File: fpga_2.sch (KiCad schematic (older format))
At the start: 1 part

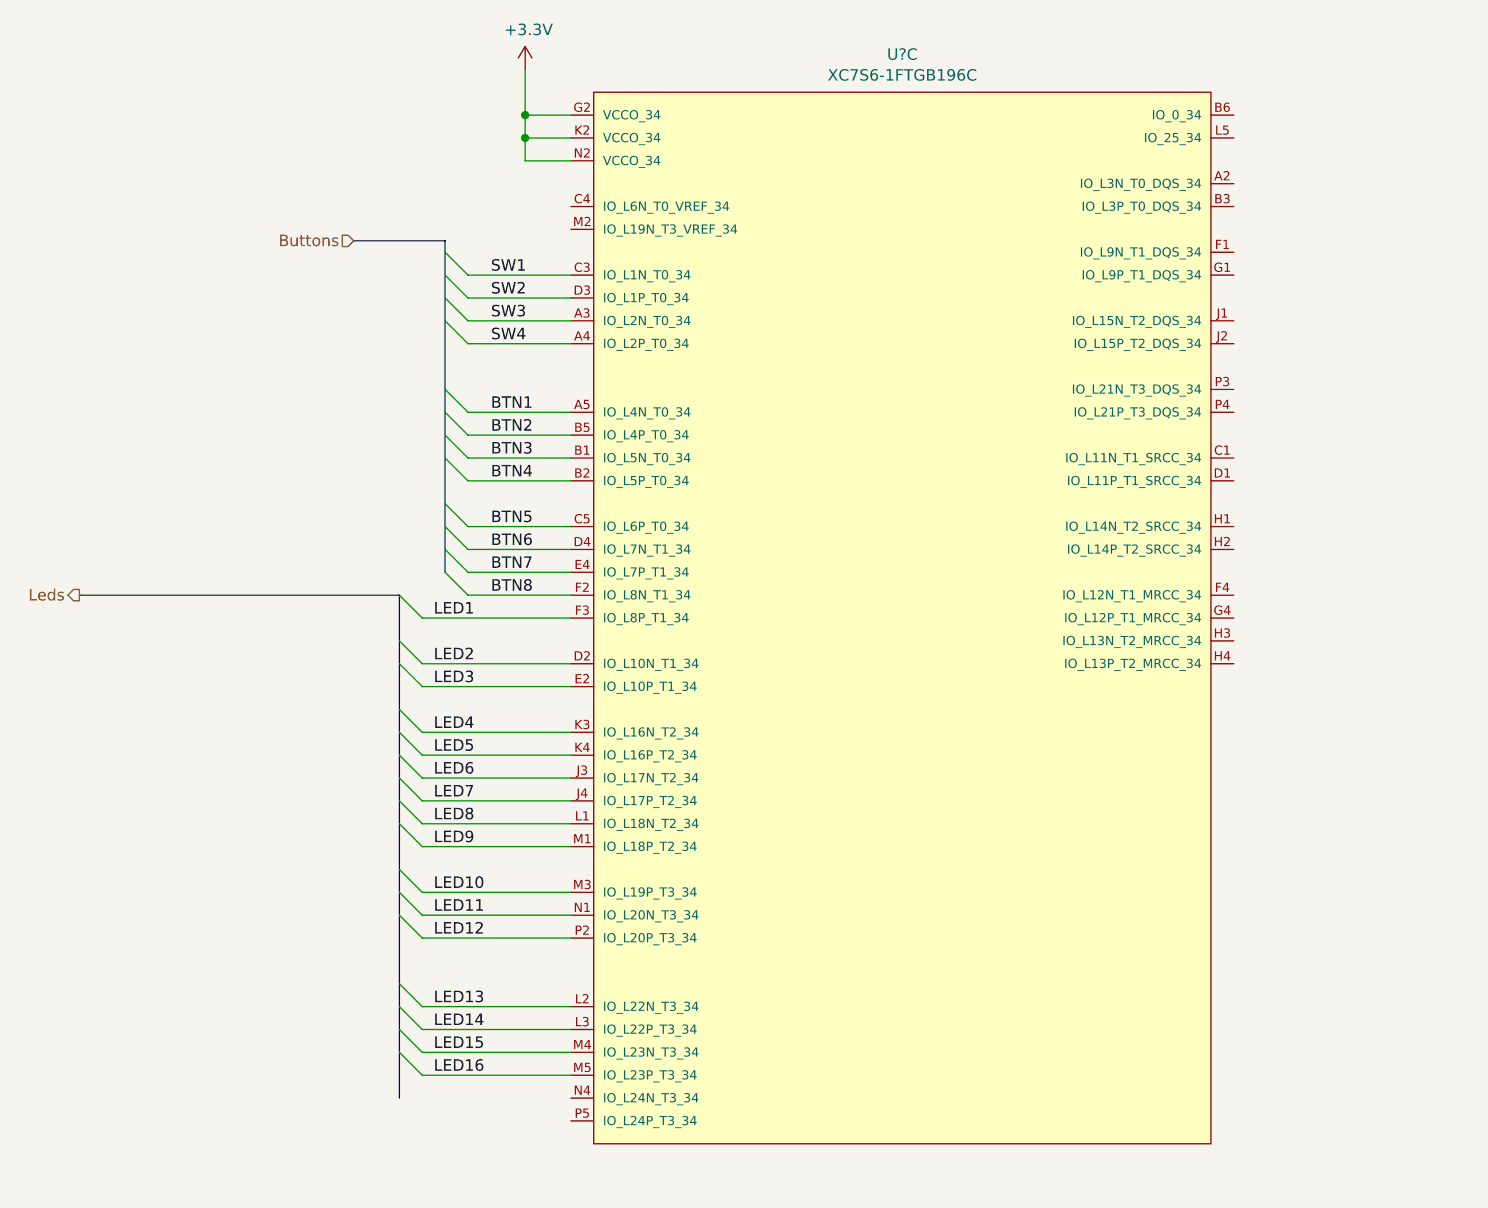
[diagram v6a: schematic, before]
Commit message: Connect USB buses to the FPGA
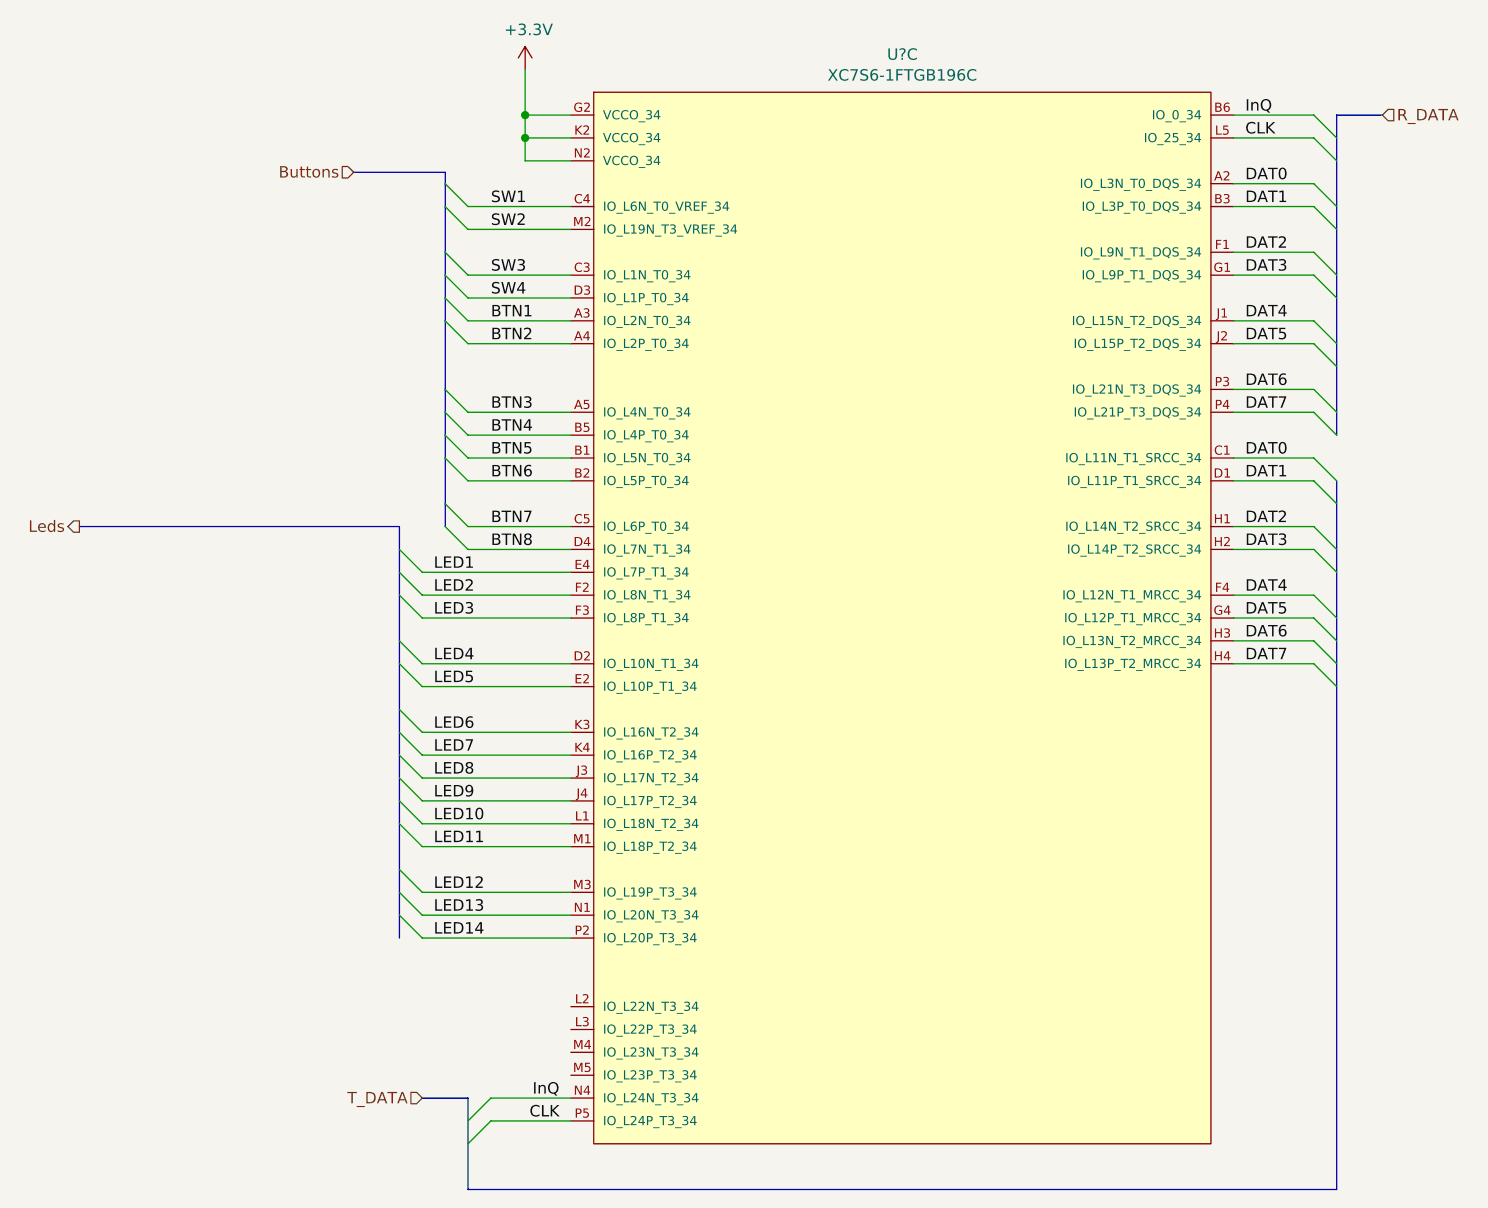
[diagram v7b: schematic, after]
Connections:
- net BTN1: now also U?.A3 (IO_L2N_T0_34); no longer U?.A5 (IO_L4N_T0_34)
- net BTN2: now also U?.A4 (IO_L2P_T0_34); no longer U?.B5 (IO_L4P_T0_34)
- net BTN3: now also U?.A5 (IO_L4N_T0_34); no longer U?.B1 (IO_L5N_T0_34)
- net BTN4: now also U?.B5 (IO_L4P_T0_34); no longer U?.B2 (IO_L5P_T0_34)
- net BTN5: now also U?.B1 (IO_L5N_T0_34); no longer U?.C5 (IO_L6P_T0_34)
- net BTN6: now also U?.B2 (IO_L5P_T0_34); no longer U?.D4 (IO_L7N_T1_34)
- net BTN7: now also U?.C5 (IO_L6P_T0_34); no longer U?.E4 (IO_L7P_T1_34)
- net BTN8: now also U?.D4 (IO_L7N_T1_34); no longer U?.F2 (IO_L8N_T1_34)
- net LED1: now also U?.E4 (IO_L7P_T1_34); no longer U?.F3 (IO_L8P_T1_34)
- net LED10: now also U?.L1 (IO_L18N_T2_34); no longer U?.M3 (IO_L19P_T3_34)
- net LED11: now also U?.M1 (IO_L18P_T2_34); no longer U?.N1 (IO_L20N_T3_34)
- net LED12: now also U?.M3 (IO_L19P_T3_34); no longer U?.P2 (IO_L20P_T3_34)
- net LED13: now also U?.N1 (IO_L20N_T3_34); no longer U?.L2 (IO_L22N_T3_34)
- net LED14: now also U?.P2 (IO_L20P_T3_34); no longer U?.L3 (IO_L22P_T3_34)
- net LED2: now also U?.F2 (IO_L8N_T1_34); no longer U?.D2 (IO_L10N_T1_34)
- net LED3: now also U?.F3 (IO_L8P_T1_34); no longer U?.E2 (IO_L10P_T1_34)
- net LED4: now also U?.D2 (IO_L10N_T1_34); no longer U?.K3 (IO_L16N_T2_34)
- net LED5: now also U?.E2 (IO_L10P_T1_34); no longer U?.K4 (IO_L16P_T2_34)
- net LED6: now also U?.K3 (IO_L16N_T2_34); no longer U?.J3 (IO_L17N_T2_34)
- net LED7: now also U?.K4 (IO_L16P_T2_34); no longer U?.J4 (IO_L17P_T2_34)
- net LED8: now also U?.J3 (IO_L17N_T2_34); no longer U?.L1 (IO_L18N_T2_34)
- net LED9: now also U?.J4 (IO_L17P_T2_34); no longer U?.M1 (IO_L18P_T2_34)
- net SW1: now also U?.C4 (IO_L6N_T0_VREF_34); no longer U?.C3 (IO_L1N_T0_34)
- net SW2: now also U?.M2 (IO_L19N_T3_VREF_34); no longer U?.D3 (IO_L1P_T0_34)
- net SW3: now also U?.C3 (IO_L1N_T0_34); no longer U?.A3 (IO_L2N_T0_34)
- net SW4: now also U?.D3 (IO_L1P_T0_34); no longer U?.A4 (IO_L2P_T0_34)
- net DAT0: now reaches U?.A2 (IO_L3N_T0_DQS_34)
- net DAT0: now also U?.C1 (IO_L11N_T1_SRCC_34)
- net DAT1: now reaches U?.B3 (IO_L3P_T0_DQS_34)
- net DAT1: now also U?.D1 (IO_L11P_T1_SRCC_34)
- net InQ: now reaches U?.B6 (IO_0_34)
- net InQ: now also U?.N4 (IO_L24N_T3_34)
- net DAT2: now reaches U?.F1 (IO_L9N_T1_DQS_34)
- net DAT2: now also U?.H1 (IO_L14N_T2_SRCC_34)
- net DAT4: now reaches U?.F4 (IO_L12N_T1_MRCC_34)
- net DAT4: now also U?.J1 (IO_L15N_T2_DQS_34)
- net DAT3: now reaches U?.G1 (IO_L9P_T1_DQS_34)
- net DAT3: now also U?.H2 (IO_L14P_T2_SRCC_34)
- net DAT5: now reaches U?.G4 (IO_L12P_T1_MRCC_34)
- net DAT5: now also U?.J2 (IO_L15P_T2_DQS_34)
- net DAT6: now reaches U?.H3 (IO_L13N_T2_MRCC_34)
- net DAT6: now also U?.P3 (IO_L21N_T3_DQS_34)
- net DAT7: now reaches U?.H4 (IO_L13P_T2_MRCC_34)
- net DAT7: now also U?.P4 (IO_L21P_T3_DQS_34)
- net CLK: now reaches U?.L5 (IO_25_34)
- net CLK: now also U?.P5 (IO_L24P_T3_34)
- net LED15: no longer names the net of U?.M4 (IO_L23N_T3_34)
- net LED16: no longer names the net of U?.M5 (IO_L23P_T3_34)
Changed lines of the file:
@@
 Wire Wire Line
 	4450 1600 4450 1400
-Text HLabel 3700 2150 0    50   Input ~ 0
+Text HLabel 3700 1850 0    50   Input ~ 0
 Buttons
 Wire Bus Line
-	3700 2150 4100 2150
+	3700 1850 4100 1850
+Entry Wire Line
+	4100 2000 4200 2100
+Entry Wire Line
+	4100 1900 4200 2000
+Entry Wire Line
+	4100 2200 4200 2300
 Entry Wire Line
 	4100 2300 4200 2400
 Entry Wire Line
-	4100 2200 4200 2300
-Entry Wire Line
 	4100 2400 4200 2500
 Entry Wire Line
 	4100 2500 4200 2600
+Wire Wire Line
+	4200 2000 4650 2000
+Wire Wire Line
+	4200 2100 4650 2100
+Wire Wire Line
+	4200 2300 4650 2300
+Wire Wire Line
+	4200 2400 4650 2400
+Wire Wire Line
+	4200 2500 4650 2500
+Wire Wire Line
+	4200 2600 4650 2600
+Text Label 4300 2000 0    50   ~ 0
+SW1
+Text Label 4300 2100 0    50   ~ 0
+SW2
+Text Label 4300 2300 0    50   ~ 0
+SW3
+Text Label 4300 2400 0    50   ~ 0
+SW4
+Text Label 4300 2500 0    50   ~ 0
+BTN1
+Text Label 4300 2600 0    50   ~ 0
+BTN2
 Entry Wire Line
 	4100 2800 4200 2900
 Entry Wire Line
 	4100 2900 4200 3000
-Wire Wire Line
-	4200 2300 4650 2300
-Wire Wire Line
-	4200 2400 4650 2400
-Wire Wire Line
-	4200 2500 4650 2500
-Wire Wire Line
-	4200 2600 4650 2600
+Entry Wire Line
+	4100 3000 4200 3100
+Entry Wire Line
+	4100 3100 4200 3200
+Entry Wire Line
+	4100 3300 4200 3400
+Entry Wire Line
+	4100 3400 4200 3500
 Wire Wire Line
 	4200 2900 4650 2900
 Wire Wire Line
 	4200 3000 4650 3000
-Text Label 4300 2300 0    50   ~ 0
-SW1
-Text Label 4300 2400 0    50   ~ 0
-SW2
-Text Label 4300 2500 0    50   ~ 0
-SW3
-Text Label 4300 2600 0    50   ~ 0
-SW4
+Wire Wire Line
+	4200 3100 4650 3100
+Wire Wire Line
+	4200 3200 4650 3200
+Wire Wire Line
+	4200 3400 4650 3400
+Wire Wire Line
+	4200 3500 4650 3500
 Text Label 4300 2900 0    50   ~ 0
-BTN1
+BTN3
 Text Label 4300 3000 0    50   ~ 0
-BTN2
-Entry Wire Line
-	4100 3000 4200 3100
-Entry Wire Line
-	4100 3100 4200 3200
-Entry Wire Line
-	4100 3300 4200 3400
-Entry Wire Line
-	4100 3400 4200 3500
-Entry Wire Line
-	4100 3500 4200 3600
-Entry Wire Line
-	4100 3600 4200 3700
-Wire Wire Line
-	4200 3100 4650 3100
-Wire Wire Line
-	4200 3200 4650 3200
-Wire Wire Line
-	4200 3400 4650 3400
-Wire Wire Line
-	4200 3500 4650 3500
-Wire Wire Line
-	4200 3600 4650 3600
-Wire Wire Line
-	4200 3700 4650 3700
+BTN4
 Text Label 4300 3100 0    50   ~ 0
-BTN3
+BTN5
 Text Label 4300 3200 0    50   ~ 0
-BTN4
+BTN6
 Text Label 4300 3400 0    50   ~ 0
-BTN5
+BTN7
 Text Label 4300 3500 0    50   ~ 0
-BTN6
-Text Label 4300 3600 0    50   ~ 0
-BTN7
-Text Label 4300 3700 0    50   ~ 0
 BTN8
 Wire Bus Line
-	2500 3700 3900 3700
+	2500 3400 3900 3400
+Entry Wire Line
+	3900 3500 4000 3600
+Wire Wire Line
+	4000 3600 4650 3600
+Entry Wire Line
+	3900 3600 4000 3700
+Wire Wire Line
+	4000 3700 4650 3700
 Entry Wire Line
 	3900 3700 4000 3800
@@
 Wire Wire Line
 	4000 5200 4650 5200
-Entry Wire Line
-	3900 5400 4000 5500
-Wire Wire Line
-	4000 5500 4650 5500
-Entry Wire Line
-	3900 5500 4000 5600
-Wire Wire Line
-	4000 5600 4650 5600
+Text Label 4050 3600 0    50   ~ 0
+LED1
+Text Label 4050 3700 0    50   ~ 0
+LED2
 Text Label 4050 3800 0    50   ~ 0
-LED1
+LED3
 Text Label 4050 4000 0    50   ~ 0
-LED2
+LED4
 Text Label 4050 4100 0    50   ~ 0
-LED3
+LED5
 Text Label 4050 4300 0    50   ~ 0
-LED4
+LED6
 Text Label 4050 4400 0    50   ~ 0
-LED5
+LED7
 Text Label 4050 4500 0    50   ~ 0
-LED6
+LED8
 Text Label 4050 4600 0    50   ~ 0
-LED7
+LED9
 Text Label 4050 4700 0    50   ~ 0
-LED8
+LED10
 Text Label 4050 4800 0    50   ~ 0
-LED9
+LED11
 Text Label 4050 5000 0    50   ~ 0
-LED10
+LED12
 Text Label 4050 5100 0    50   ~ 0
-LED11
+LED13
 Text Label 4050 5200 0    50   ~ 0
-LED12
-Text Label 4050 5500 0    50   ~ 0
-LED13
-Text Label 4050 5600 0    50   ~ 0
 LED14
-Text HLabel 2500 3700 0    50   Output ~ 0
+Text HLabel 2500 3400 0    50   Output ~ 0
 Leds
 Entry Wire Line
-	3900 5600 4000 5700
-Entry Wire Line
-	3900 5700 4000 5800
-Wire Wire Line
-	4000 5800 4650 5800
-Wire Wire Line
-	4000 5700 4650 5700
-Wire Bus Line
-	4100 2150 4100 3600
-Wire Bus Line
-	3900 3700 3900 5900
-Text Label 4050 5700 0    50   ~ 0
-LED15
-Text Label 4050 5800 0    50   ~ 0
-LED16
+	7900 3100 8000 3200
+Entry Wire Line
+	7900 3200 8000 3300
+Entry Wire Line
+	7900 3400 8000 3500
+Wire Wire Line
+	7550 3100 7900 3100
+Wire Wire Line
+	7550 3200 7900 3200
+Wire Wire Line
+	7550 3400 7900 3400
+Wire Wire Line
+	7550 3500 7900 3500
+Text Label 7600 3100 0    50   ~ 0
+DAT0
+Text Label 7600 3200 0    50   ~ 0
+DAT1
+Text Label 7600 3400 0    50   ~ 0
+DAT2
+Text Label 7600 3500 0    50   ~ 0
+DAT3
+Wire Wire Line
+	4650 6000 4300 6000
+Entry Wire Line
+	4300 6000 4200 6100
+Text Label 4600 6000 2    50   ~ 0
+CLK
+Wire Wire Line
+	4650 5900 4300 5900
+Entry Wire Line
+	4300 5900 4200 6000
+Text Label 4600 5900 2    50   ~ 0
+InQ
+Wire Bus Line
+	4200 5900 4000 5900
+Text HLabel 4000 5900 0    50   Input ~ 0
+T_DATA
+Entry Wire Line
+	7900 1900 8000 2000
+Entry Wire Line
+	7900 2000 8000 2100
+Entry Wire Line
+	7900 2200 8000 2300
+Entry Wire Line
+	7900 2300 8000 2400
+Entry Wire Line
+	7900 2500 8000 2600
+Entry Wire Line
+	7900 2600 8000 2700
+Entry Wire Line
+	7900 2800 8000 2900
+Entry Wire Line
+	7900 2900 8000 3000
+Wire Wire Line
+	7550 1900 7900 1900
+Wire Wire Line
+	7550 2000 7900 2000
+Wire Wire Line
+	7550 2200 7900 2200
+Wire Wire Line
+	7550 2300 7900 2300
+Wire Wire Line
+	7550 2500 7900 2500
+Wire Wire Line
+	7550 2600 7900 2600
+Wire Wire Line
+	7550 2800 7900 2800
+Wire Wire Line
+	7550 2900 7900 2900
+Text Label 7600 1900 0    50   ~ 0
+DAT0
+Text Label 7600 2000 0    50   ~ 0
+DAT1
+Text Label 7600 2200 0    50   ~ 0
+DAT2
+Text Label 7600 2300 0    50   ~ 0
+DAT3
+Text Label 7600 2500 0    50   ~ 0
+DAT4
+Text Label 7600 2600 0    50   ~ 0
+DAT5
+Text Label 7600 2800 0    50   ~ 0
+DAT6
+Text Label 7600 2900 0    50   ~ 0
+DAT7
+Wire Wire Line
+	7550 1700 7900 1700
+Entry Wire Line
+	7900 1700 8000 1800
+Text Label 7600 1700 0    50   ~ 0
+CLK
+Wire Wire Line
+	7550 1600 7900 1600
+Entry Wire Line
+	7900 1600 8000 1700
+Text Label 7600 1600 0    50   ~ 0
+InQ
+Wire Bus Line
+	8000 1600 8200 1600
+Text HLabel 8200 1600 2    50   Input ~ 0
+R_DATA
+Text Label 7600 4000 0    50   ~ 0
+DAT7
+Text Label 7600 3900 0    50   ~ 0
+DAT6
+Text Label 7600 3800 0    50   ~ 0
+DAT5
+Text Label 7600 3700 0    50   ~ 0
+DAT4
+Wire Wire Line
+	7550 4000 7900 4000
+Wire Wire Line
+	7550 3900 7900 3900
+Wire Wire Line
+	7550 3800 7900 3800
+Wire Wire Line
+	7550 3700 7900 3700
+Entry Wire Line
+	7900 4000 8000 4100
+Entry Wire Line
+	7900 3900 8000 4000
+Entry Wire Line
+	7900 3800 8000 3900
+Entry Wire Line
+	7900 3700 8000 3800
+Entry Wire Line
+	7900 3500 8000 3600
+Wire Bus Line
+	8000 6300 4200 6300
+Wire Bus Line
+	4200 5900 4200 6300
+Wire Bus Line
+	8000 1600 8000 3000
+Wire Bus Line
+	8000 3200 8000 6300
+Wire Bus Line
+	4100 1850 4100 3400
+Wire Bus Line
+	3900 3400 3900 5200
 $EndSCHEMATC

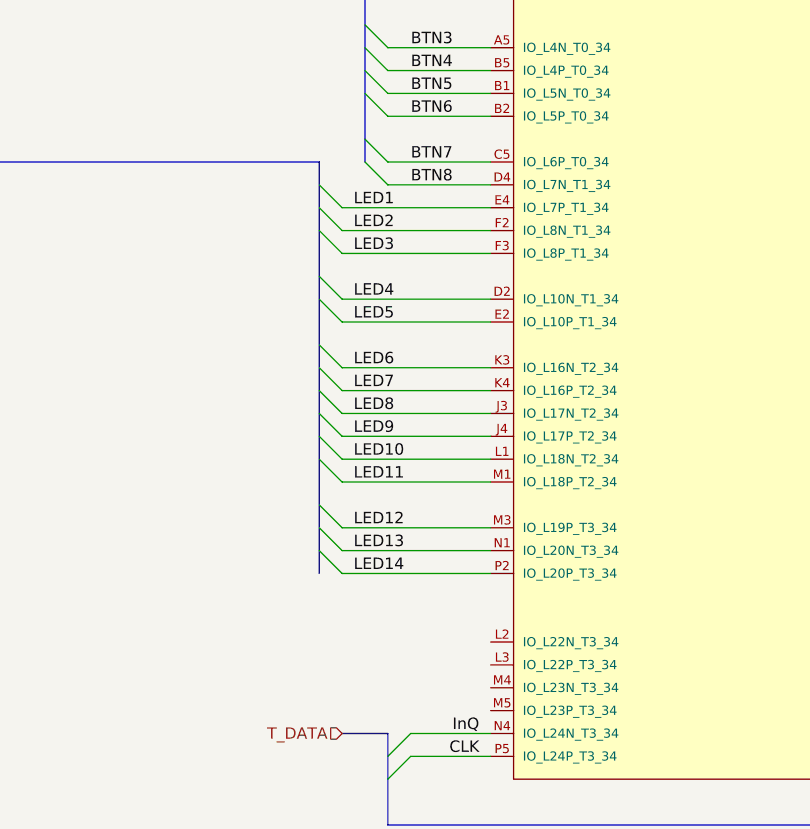
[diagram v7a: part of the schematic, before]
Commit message: Add LED15 and LED16
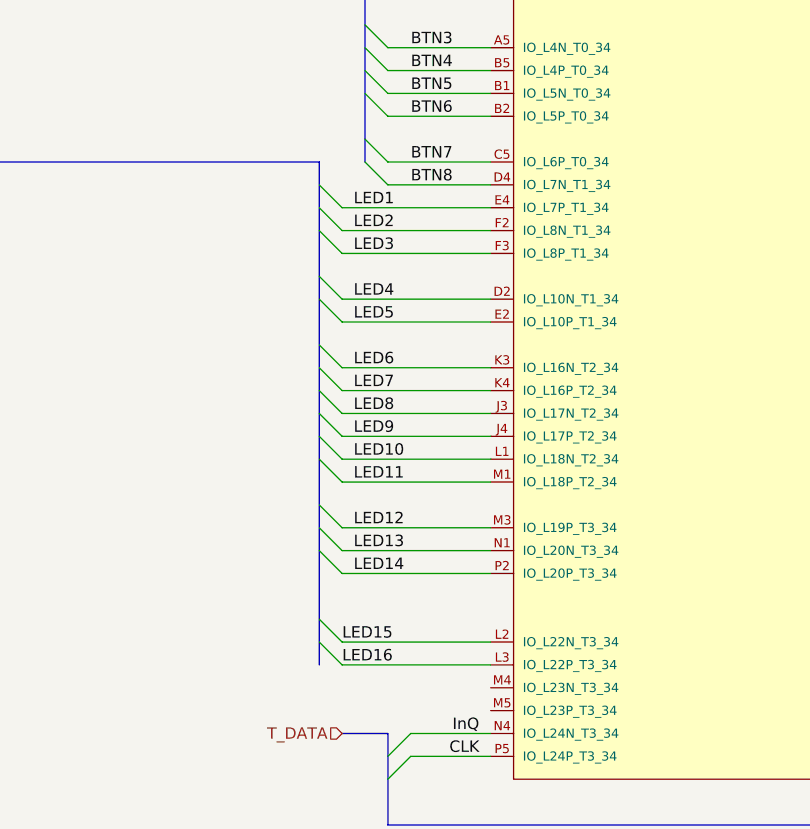
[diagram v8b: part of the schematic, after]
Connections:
- net LED15: now reaches U?.L2 (IO_L22N_T3_34)
- net LED16: now reaches U?.L3 (IO_L22P_T3_34)
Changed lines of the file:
@@
 Wire Bus Line
 	8000 6300 4200 6300
+Text Label 4000 5500 0    50   ~ 0
+LED15
+Text Label 4000 5600 0    50   ~ 0
+LED16
+Entry Wire Line
+	4000 5500 3900 5400
+Entry Wire Line
+	3900 5500 4000 5600
+Wire Wire Line
+	4650 5500 4000 5500
+Wire Wire Line
+	4000 5600 4650 5600
 Wire Bus Line
 	4200 5900 4200 6300
@@
 	4100 1850 4100 3400
 Wire Bus Line
-	3900 3400 3900 5200
+	3900 3400 3900 5600
 $EndSCHEMATC
